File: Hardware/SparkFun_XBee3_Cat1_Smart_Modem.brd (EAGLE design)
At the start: 45.7 x 63.5 mm, 141 parts, among them J1 USB Female Type C Connector, J3 USB Female Type C Connector, J4 QWIIC_RIGHT_ANGLE, Q2 3.1A/30V/105mΩ, U1 FSUSB30MUX_MSOP10, U2 AP63203, U3 ESD Diode, U5 ESD Diode, U6 CP210X

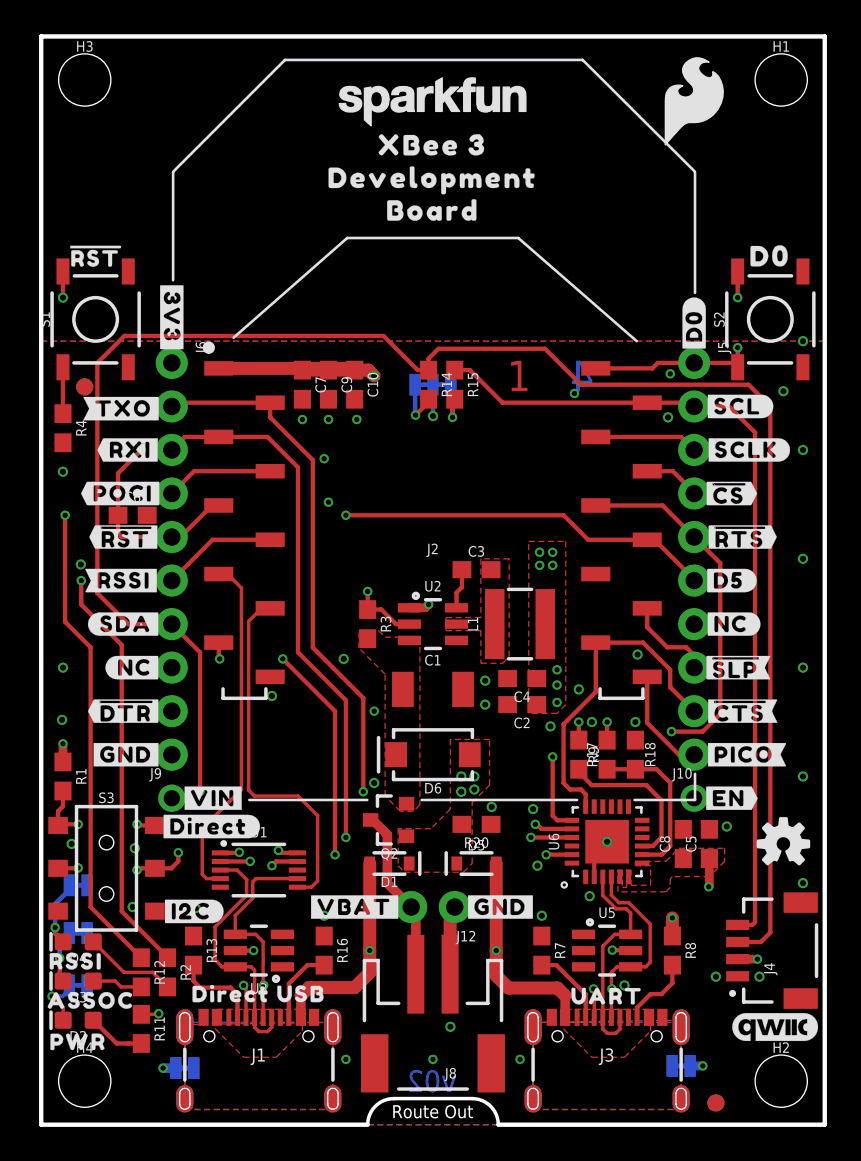
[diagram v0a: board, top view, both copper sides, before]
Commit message: Moves resistor for LEDs so that they're grouped in a better configuration
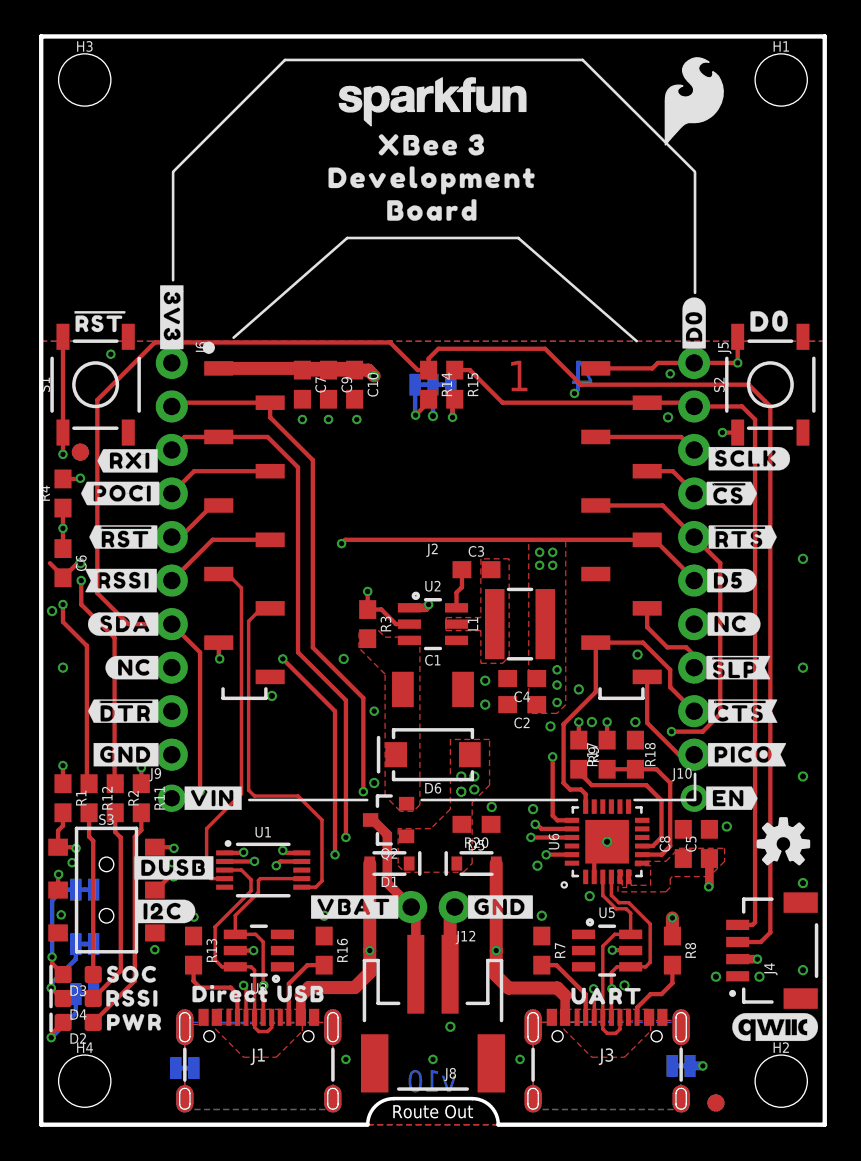
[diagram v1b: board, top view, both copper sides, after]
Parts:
- removed U$50: (no value), top:#TXO#12
- removed U$69: (no value), botmirror:#DIRECT#31
- U$32: device top:#SCL#7 -> botmirror:#DUSB#31
- U$43: device top:ASSOC27 -> topmirror:SOC30
- moved U$32 42.5 mm to (7.75, 15.0)
- moved R11 13.5 mm to (5.84, 19.1)
- moved R2 10.6 mm to (4.32, 19.1)
- moved R12 10.6 mm to (2.79, 19.1)
- moved U$64 5.21 mm to (5.97, 13.7), turned to 0 degrees
- moved C6 4.93 mm to (1.27, 32.8), turned to 270 degrees
- moved U$62 3.95 mm to (5.33, 7.37)
- moved U$30 3.82 mm to (3.43, 46.9)
- moved FD1 3.82 mm to (2.29, 39.2)
- moved FD2 3.82 mm to (2.29, 39.2)
- moved R4 3.81 mm to (1.27, 36.8), turned to 90 degrees
- moved S1 3.81 mm to (3.17, 43.2)
- moved S2 3.81 mm to (42.5, 43.2)
- moved U$40 3.81 mm to (42.5, 46.9)
- moved U$42 3.49 mm to (5.46, 5.97)
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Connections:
- net N$21 renamed ALED
- net N$23 renamed PLED
- net N$3 renamed RLED
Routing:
- net D5/ASSOCIATE: track 66.9 -> 52.8 mm
- net D10/RSSI_PWM: track 36.2 -> 25.1 mm
- net N$7: track 3.44 -> 13.5 mm
- net N$12: track 2.95 -> 9.54 mm
- net !RESET!: track 30.1 -> 23.6 mm
- net N$2: track 5.42 -> 11.6 mm
- net ALED: track 3.11 -> 6.23 mm
- net DIRECT_SELECT: track 12.6 -> 14.9 mm, vias 4 -> 3
- net D11/SDA: track 112.3 -> 110.5 mm
- net FIRMWARE: track 8.26 -> 10.1 mm
- net GND: track 10.5 -> 12.3 mm, vias 53 -> 49
- net PLED: track 3.08 -> 4.31 mm
- net D0: track 14.1 -> 15.3 mm
- net 3.3V: track 31.0 -> 31.9 mm, vias 16 -> 17
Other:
- board text added: "v10"
- board text removed: "v02"

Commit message: Fixes silk, aligns some text in the schematic, adds ordering instructions
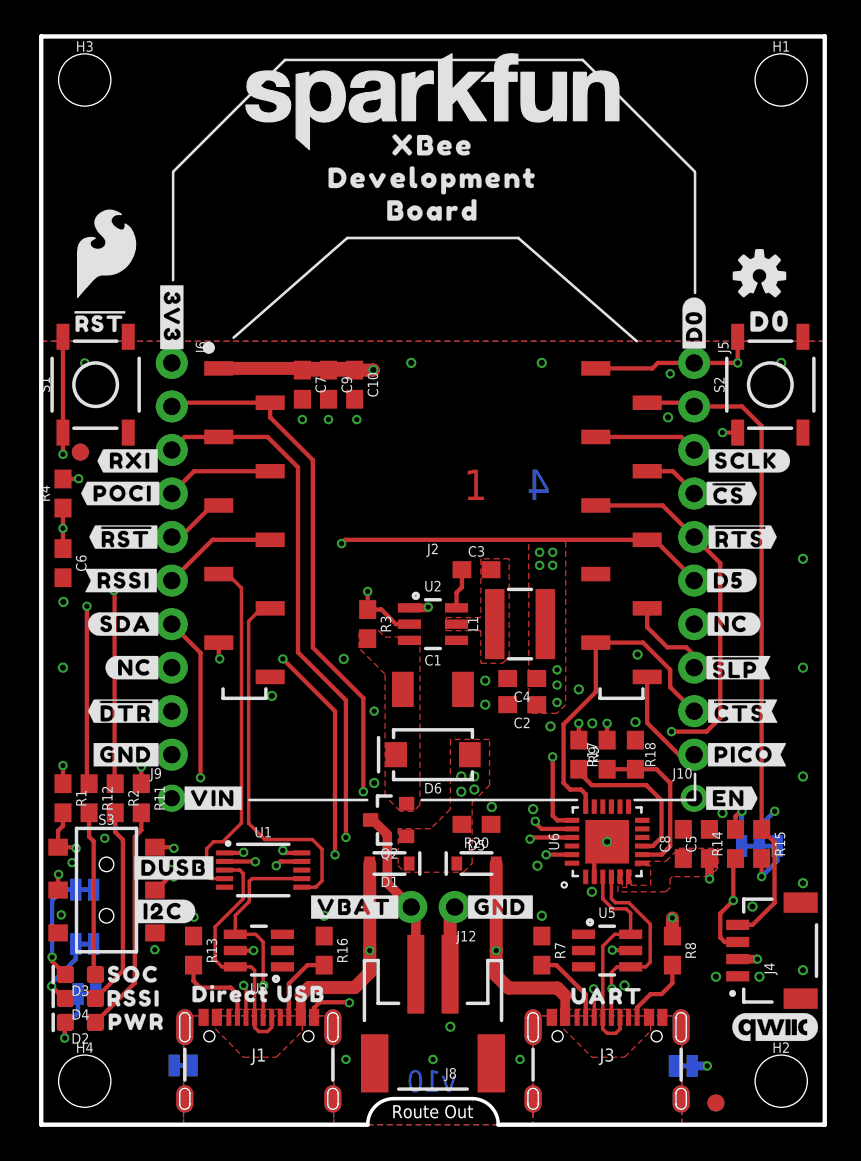
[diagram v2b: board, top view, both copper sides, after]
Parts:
- removed U$53: (no value), top:XBEE_335
- added LOGO5: SPECIAL_INSTRUCTIONS-ORDERING, SparkFun-Aesthetics:ORDERING_INSTRUCTIONS
- added U$50: (no value), top:XBEE339
- LOGO1: value SFE_LOGO_NAME.1_INCH -> SFE_LOGO_NAME.2_INCH; device SparkFun-Aesthetics:SFE_LOGO_NAME_.1 -> SparkFun-Aesthetics:SFE_LOGO_NAME_.2
- U$23: device top:XBEE_335 -> top:XBEE339
- U$6: device top:#D2#AD2#19 -> top:#D1#AD1#SDA#8
- moved U$26 35.9 mm to (41.9, 14.5)
- moved U$61 35.4 mm to (3.81, 50.8)
- moved LOGO2 33.2 mm to (41.9, 49.5)
- moved I2C_PU 33.0 mm to (41.9, 16.3)
- moved R14 32.2 mm to (40.5, 16.4), turned to 90 degrees
- moved R15 32.2 mm to (42.0, 16.4)
- moved U$6 1.65 mm to (32.3, 39.4)
- moved U$63 1.27 mm to (22.9, 48.3)
- moved U$70 1.27 mm to (22.9, 37.5)
- moved U$71 1.27 mm to (22.9, 35.6)
- moved U$35 0.25 mm to (34.0, 3.43)
- moved SHLD1 0.18 mm to (8.28, 3.45)
- moved U$36 0.18 mm to (12.1, 3.43)
- moved SHLD 0.13 mm to (37.5, 3.43)
- moved U$33 0.13 mm to (41.1, 38.7)
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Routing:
- net D11/SDA: track 110.5 -> 55.3 mm, vias 2 -> 3
- net D1/SCL: track 49.1 -> 38.1 mm
- net D10/RSSI_PWM: track 25.1 -> 21.6 mm
- net D5/ASSOCIATE: track 52.8 -> 49.9 mm
- net EN: track 44.0 -> 45.9 mm
- net VIN: track 26.6 -> 28.2 mm, vias 6 -> 5
- net D13/TXO: track 44.8 -> 44.1 mm
- net GND: track 12.3 -> 12.7 mm, vias 49 -> 53
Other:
- board text added: "1.6mm Thickness"
- board text added: "FOUR LAYER BOARD"
- board text added: "LEAD-FREE HASL"

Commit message: Fixes a number of labels
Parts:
- removed U$59: (no value), top:#D8##DTR##26
- added U$53: (no value), top:#D8##DTR##27
- U$19: device top:#D1#AD1#8 -> top:#D2#AD2#19
- U$6: device top:#D1#AD1#SDA#8 -> top:#D1#AD1#SCL#8
- moved U$50 17.8 mm to (22.9, 57.1)
- moved U$71 17.8 mm to (22.9, 53.3)
- moved U$70 17.8 mm to (22.9, 55.2)
- moved U$63 11.5 mm to (21.6, 59.7)
- moved U$19 2.68 mm to (34.0, 39.2)
- moved U$6 2.55 mm to (32.5, 41.9)
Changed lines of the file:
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@@
 <drawing>
 <settings>
-<setting alwaysvectorfont="no"/>
+<setting alwaysvectorfont="yes"/>
 <setting verticaltext="up"/>
 </settings>
@@
 <element name="U$57" library="top" package="#D6##RTS##24" value="" x="34.036" y="34.29" smashed="yes" rot="MR0"/>
 <element name="U$58" library="top" package="#D7##CTS##25" value="" x="34.036" y="24.13" smashed="yes" rot="MR0"/>
-<element name="U$59" library="top" package="#D8##DTR##26" value="" x="11.557" y="24.13" smashed="yes" rot="MR0"/>
 <element name="U$60" library="top" package="#D9##SLP##27" value="" x="34.29" y="26.67" smashed="yes" rot="MR0"/>
 <element name="U$15" library="top" package="#TXO#D13#13" value="" x="12.192" y="41.91" smashed="yes" rot="MR0"/>
@@
 <element name="U$65" library="top" package="UART32" value="" x="33.02" y="7.493" smashed="yes"/>
 <element name="U$30" library="top" package="#RST#30" value="" x="3.429" y="46.863" smashed="yes"/>
-<element name="U$63" library="SparkFun-Aesthetics" package="SFE_LOGO_NAME_.2" value="" x="22.86" y="48.26" smashed="yes" rot="MR0"/>
+<element name="U$63" library="SparkFun-Aesthetics" package="SFE_LOGO_NAME_.2" value="" x="21.59" y="59.69" smashed="yes" rot="MR0"/>
 <element name="U$61" library="SparkFun-Aesthetics" package="SFE_LOGO_FLAME_.2" value="" x="3.81" y="50.8" smashed="yes"/>
 <element name="D4" library="SparkFun-LED" package="LED-0603" value="BLUE" x="2.286" y="7.366" smashed="yes" rot="R180">
@@
 <element name="U$62" library="top" package="RSSI31" value="" x="5.4102" y="7.366" smashed="yes"/>
 <element name="U$64" library="top" package="#RLED#22" value="" x="5.969" y="13.716" smashed="yes" rot="MR0"/>
-<element name="U$19" library="top" package="#D1#AD1#8" value="" x="34.29" y="41.91" smashed="yes" rot="MR0"/>
 <element name="U$14" library="top" package="#POCI#D12#24" value="" x="12.319" y="36.83" smashed="yes" rot="MR0"/>
 <element name="U$29" library="top" package="#POCI#23" value="" x="4.7752" y="36.83" smashed="yes"/>
@@
 <element name="U$51" library="topmirror" package="DEVELOPMENT1345" value="" x="22.86" y="55.245" smashed="yes"/>
 <element name="U$52" library="topmirror" package="BOARD1346" value="" x="22.86" y="53.34" smashed="yes"/>
-<element name="U$70" library="topmirror" package="DEVELOPMENT1345" value="" x="22.86" y="37.465" smashed="yes" rot="MR0"/>
-<element name="U$71" library="topmirror" package="BOARD1346" value="" x="22.86" y="35.56" smashed="yes" rot="MR0"/>
+<element name="U$70" library="topmirror" package="DEVELOPMENT1345" value="" x="22.86" y="55.245" smashed="yes" rot="MR0"/>
+<element name="U$71" library="topmirror" package="BOARD1346" value="" x="22.86" y="53.34" smashed="yes" rot="MR0"/>
 <element name="U$32" library="botmirror" package="#DUSB#31" value="" x="7.747" y="14.986" smashed="yes"/>
 <element name="U$43" library="topmirror" package="SOC30" value="" x="5.3848" y="8.763" smashed="yes"/>
-<element name="U$6" library="top" package="#D1#AD1#SDA#8" value="" x="32.258" y="39.37" smashed="yes" rot="MR0"/>
-<element name="U$50" library="top" package="XBEE339" value="" x="22.86" y="39.37" smashed="yes" rot="MR0"/>
+<element name="U$50" library="top" package="XBEE339" value="" x="22.86" y="57.15" smashed="yes" rot="MR0"/>
 <element name="U$23" library="top" package="XBEE339" value="" x="22.86" y="57.15" smashed="yes"/>
 <element name="LOGO1" library="SparkFun-Aesthetics" package="SFE_LOGO_NAME_.2" value="SFE_LOGO_NAME.2_INCH" x="22.86" y="59.69" smashed="yes"/>
 <element name="LOGO5" library="SparkFun-Aesthetics" package="ORDERING_INSTRUCTIONS" value="SPECIAL_INSTRUCTIONS-ORDERING" x="69.85" y="64.77" smashed="yes"/>
+<element name="U$19" library="top" package="#D2#AD2#19" value="" x="34.036" y="39.243" smashed="yes" rot="MR0"/>
+<element name="U$6" library="top" package="#D1#AD1#SCL#8" value="" x="32.512" y="41.91" smashed="yes" rot="MR0"/>
+<element name="U$53" library="top" package="#D8##DTR##27" value="" x="11.684" y="24.13" smashed="yes" rot="MR0"/>
 </elements>
 <signals>
@@
 <wire x1="10.36" y1="28.13" x2="10.36" y2="27.232" width="0.254" layer="1"/>
 <contactref element="J6" pad="9"/>
-<wire x1="7.62" y1="24.13" x2="9.398" y2="24.13" width="0.254" layer="15"/>
-<wire x1="10.414" y1="25.146" x2="10.414" y2="27.178" width="0.254" layer="15"/>
-<wire x1="9.398" y1="24.13" x2="10.414" y2="25.146" width="0.254" layer="15"/>
+<wire x1="10.414" y1="27.178" x2="10.414" y2="25.146" width="0.254" layer="2"/>
+<wire x1="10.414" y1="25.146" x2="9.398" y2="24.13" width="0.254" layer="2"/>
+<wire x1="9.398" y1="24.13" x2="7.62" y2="24.13" width="0.254" layer="2"/>
 </signal>
 <signal name="D4/SPI_PICO">

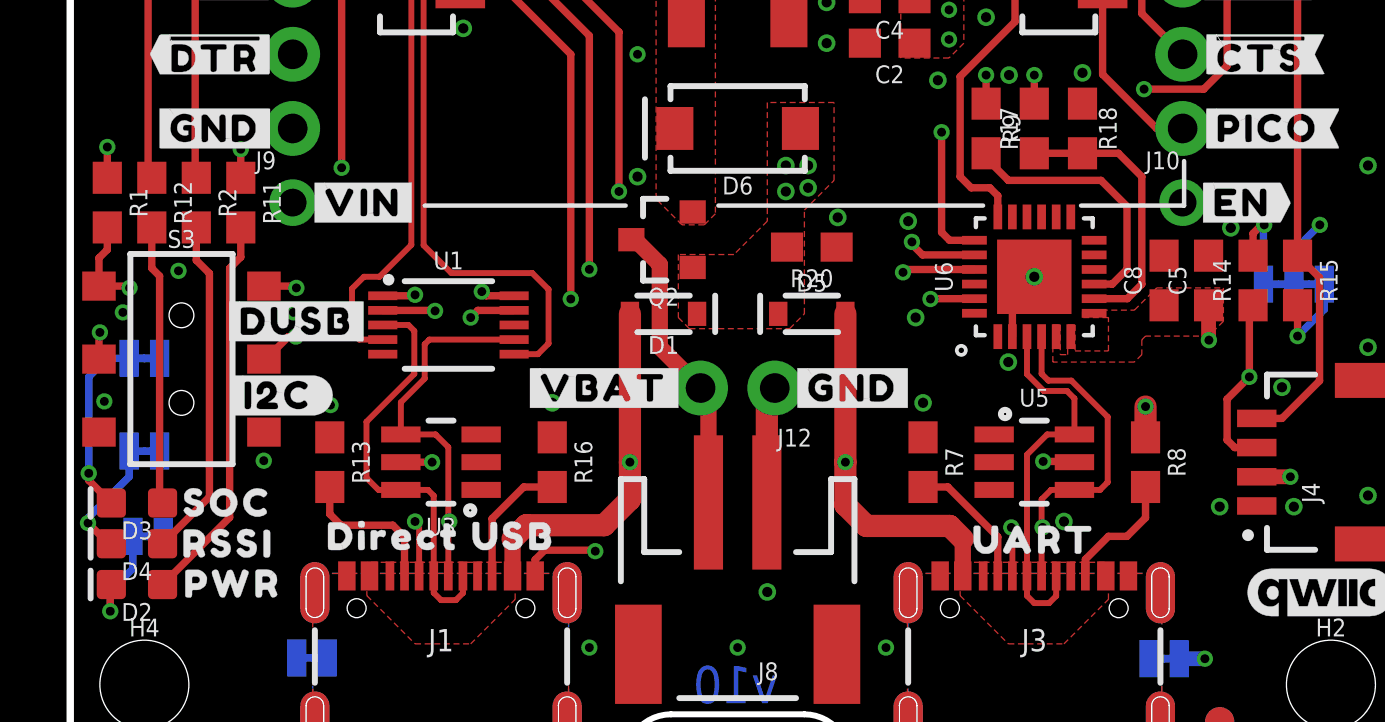
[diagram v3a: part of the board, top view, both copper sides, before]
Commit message: Updates single PTH with new footprint
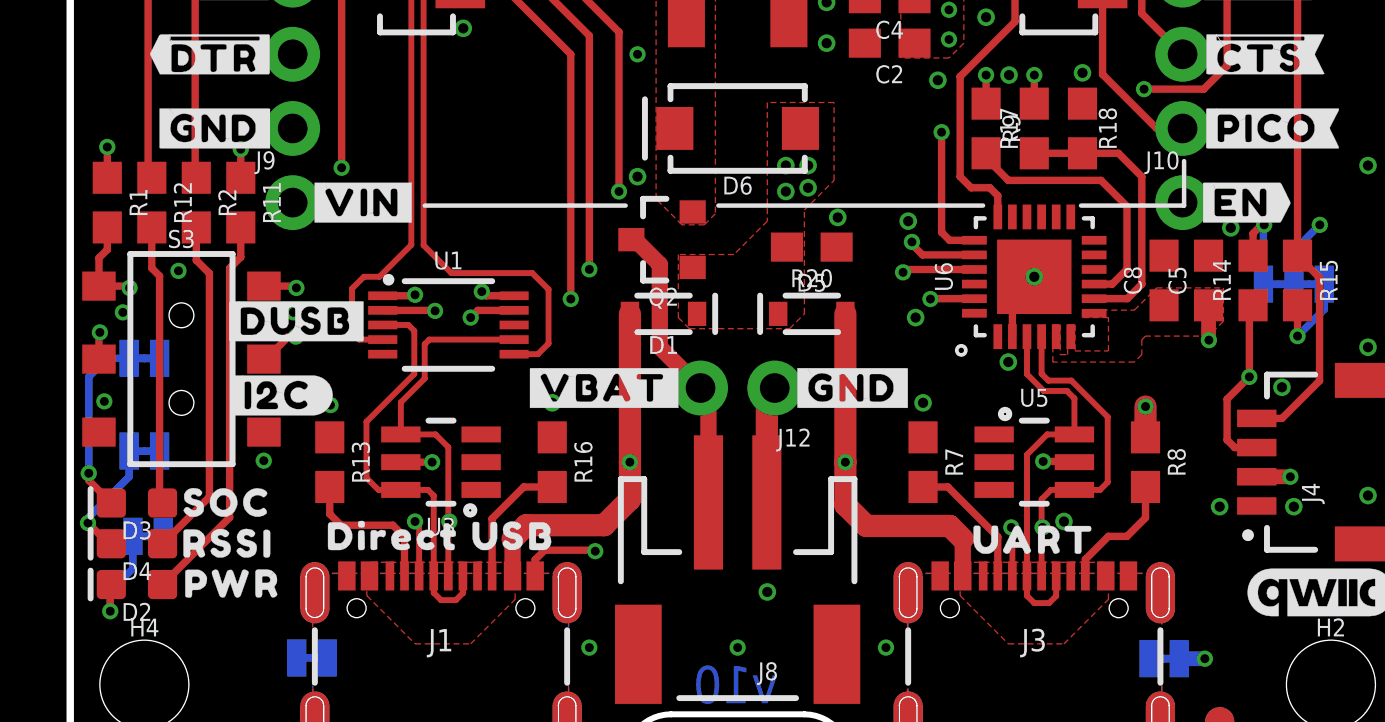
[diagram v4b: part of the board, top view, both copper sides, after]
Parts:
- J10, J9: device SparkFun-Connectors:1X01_NO_SILK -> SparkFun-Connectors:1X01_NO_SILK_STAND
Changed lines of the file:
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@@
 <drawing>
 <settings>
-<setting alwaysvectorfont="yes"/>
+<setting alwaysvectorfont="no"/>
 <setting verticaltext="up"/>
 </settings>
@@
 <layers>
 <layer number="1" name="Top" color="4" fill="1" visible="yes" active="yes"/>
-<layer number="2" name="Route2" color="23" fill="1" visible="yes" active="yes"/>
-<layer number="15" name="Route15" color="39" fill="1" visible="yes" active="yes"/>
+<layer number="2" name="Route2" color="23" fill="1" visible="no" active="yes"/>
+<layer number="15" name="Route15" color="39" fill="1" visible="no" active="yes"/>
 <layer number="16" name="Bottom" color="3" fill="1" visible="yes" active="yes"/>
 <layer number="17" name="Pads" color="26" fill="1" visible="yes" active="yes"/>
@@
 <layer number="115" name="ReferenceISLANDS" color="7" fill="1" visible="no" active="yes"/>
 <layer number="116" name="Patch_BOT" color="9" fill="4" visible="no" active="yes"/>
-<layer number="117" name="PM_Ref" color="26" fill="1" visible="no" active="yes"/>
+<layer number="117" name="PM_Ref" color="26" fill="1" visible="yes" active="yes"/>
 <layer number="118" name="Rect_Pads" color="7" fill="1" visible="no" active="yes"/>
-<layer number="119" name="PF_Ref" color="31" fill="1" visible="no" active="yes"/>
-<layer number="120" name="WFL_Ref" color="25" fill="1" visible="no" active="yes"/>
+<layer number="119" name="PF_Ref" color="31" fill="1" visible="yes" active="yes"/>
+<layer number="120" name="WFL_Ref" color="25" fill="1" visible="yes" active="yes"/>
 <layer number="121" name="_tsilk" color="7" fill="1" visible="no" active="yes"/>
 <layer number="122" name="_bsilk" color="7" fill="1" visible="no" active="yes"/>
@@
 <attribute name="VALUE" x="2.032" y="36.83" size="0.6096" layer="27" font="vector" ratio="20" rot="R90" align="top-center"/>
 </element>
-<element name="J9" library="SparkFun-Connectors" package="1X01_NO_SILK" value="" x="7.62" y="19.05" smashed="yes">
+<element name="J9" library="SparkFun-Connectors" package="1X01_NO_SILK_STAND" value="" x="7.62" y="19.05" smashed="yes">
 <attribute name="NAME" x="6.35" y="20.193" size="0.6096" layer="25" font="vector" ratio="20"/>
 <attribute name="VALUE" x="6.35" y="17.272" size="0.6096" layer="27" font="vector" ratio="20"/>
 </element>
-<element name="J10" library="SparkFun-Connectors" package="1X01_NO_SILK" value="" x="38.1" y="19.05" smashed="yes">
+<element name="J10" library="SparkFun-Connectors" package="1X01_NO_SILK_STAND" value="" x="38.1" y="19.05" smashed="yes">
 <attribute name="NAME" x="36.83" y="20.193" size="0.6096" layer="25" font="vector" ratio="20"/>
 <attribute name="VALUE" x="36.83" y="17.272" size="0.6096" layer="27" font="vector" ratio="20"/>
@@
 <contactref element="R2" pad="2"/>
 <contactref element="D4" pad="A"/>
-<wire x1="3.175" y1="7.366" x2="3.163" y2="7.366" width="0.2032" layer="1"/>
 <wire x1="4.7684" y1="16.625375" x2="4.318" y2="17.075775" width="0.254" layer="1"/>
 <wire x1="4.318" y1="17.075775" x2="4.318" y2="18.2" width="0.254" layer="1"/>
